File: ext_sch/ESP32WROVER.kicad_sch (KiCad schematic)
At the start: 4 parts, among them U4 ESP32-WROVER

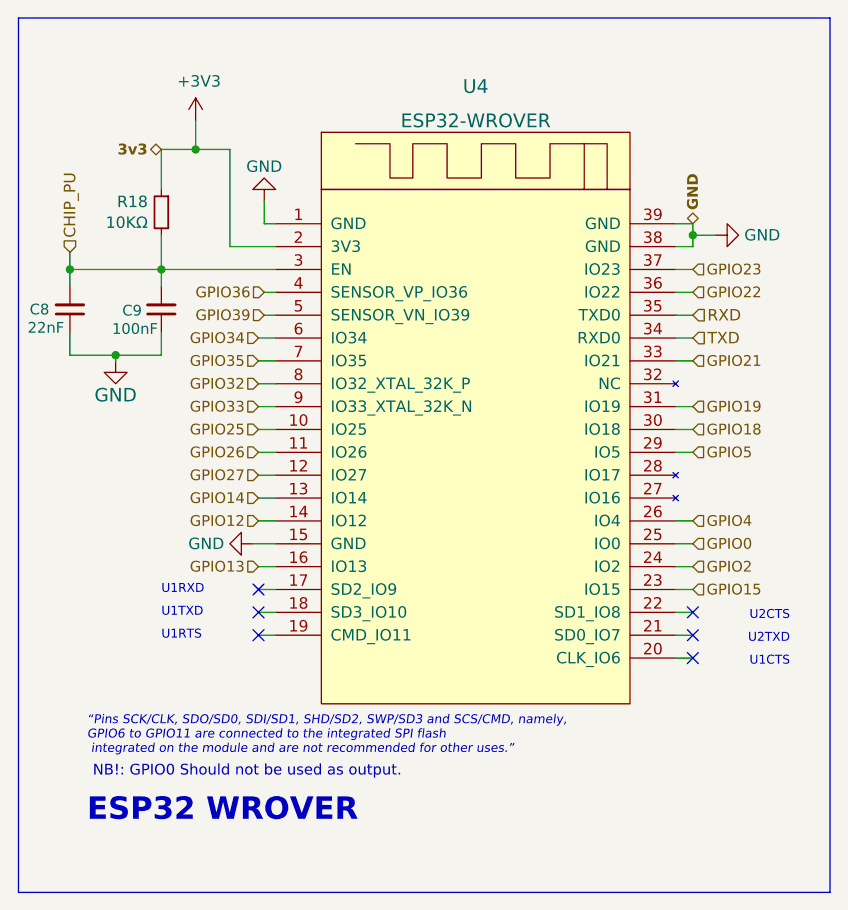
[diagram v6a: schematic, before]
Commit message: Updated all schematic values and parts numbers
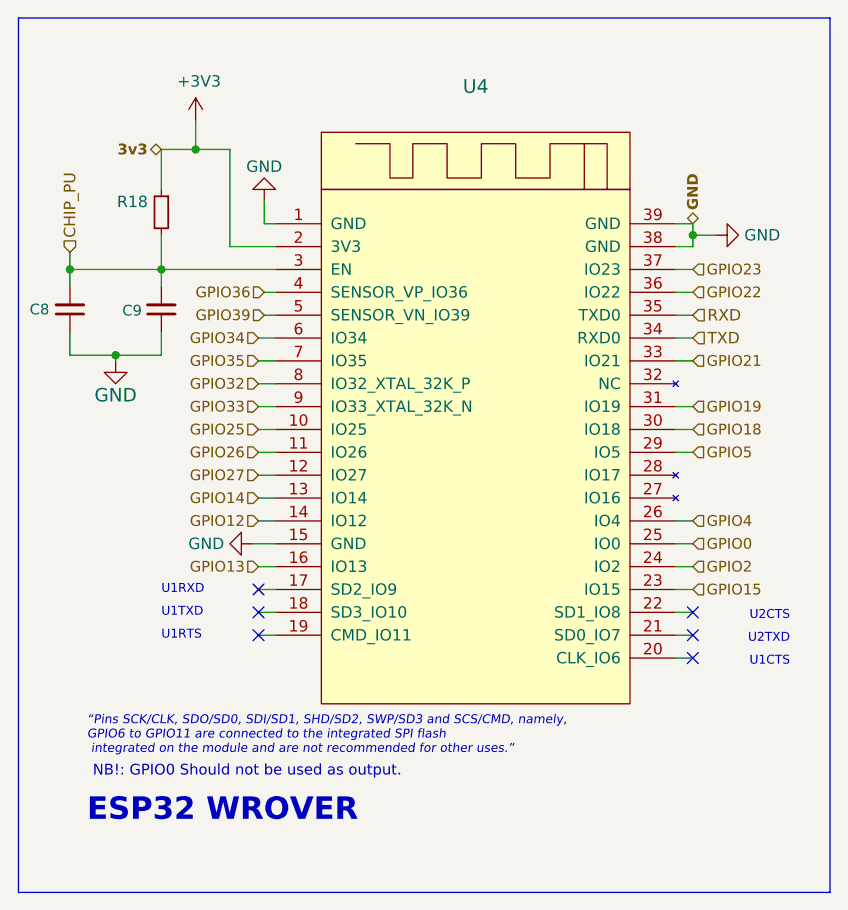
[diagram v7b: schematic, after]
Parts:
- C8: value 22nF -> (none); footprint Capacitor_SMD:C_0603_1608Metric -> (none); LCSC C106222 -> C59461
- C9: value 100nF -> (none); footprint Capacitor_SMD:C_0603_1608Metric -> (none)
- R18: value 10KΩ -> (none); footprint Resistor_SMD:R_0603_1608Metric -> (none)
- U4: value ESP32-WROVER -> (none); footprint Lib:ESP32-WROVER -> (none)
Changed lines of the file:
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@@
       (effects (font (size 1.1938 1.1938)) (justify left))
     )
-    (property "Value" "100nF" (id 1) (at 29.464 48.514 0)
+    (property "Value" "" (id 1) (at 29.464 48.514 0)
       (effects (font (size 1.1938 1.1938)) (justify left))
     )
-    (property "Footprint" "Capacitor_SMD:C_0603_1608Metric" (id 2) (at 29.845 46.355 0)
+    (property "Footprint" "" (id 2) (at 29.845 46.355 0)
       (effects (font (size 1.27 1.27)) hide)
     )
@@
       (effects (font (size 1.27 1.27)) (justify left))
     )
-    (property "Value" "10KΩ" (id 1) (at 28.3464 36.703 0)
+    (property "Value" "" (id 1) (at 28.3464 36.703 0)
       (effects (font (size 1.27 1.27)) (justify left))
     )
-    (property "Footprint" "Resistor_SMD:R_0603_1608Metric" (id 2) (at 29.845 35.56 0)
+    (property "Footprint" "" (id 2) (at 29.845 35.56 0)
       (effects (font (size 1.27 1.27)) hide)
     )
@@
       (effects (font (size 1.1938 1.1938)) (justify left))
     )
-    (property "Value" "22nF" (id 1) (at 19.05 48.387 0)
+    (property "Value" "" (id 1) (at 19.05 48.387 0)
       (effects (font (size 1.1938 1.1938)) (justify left))
     )
-    (property "Footprint" "Capacitor_SMD:C_0603_1608Metric" (id 2) (at 19.685 46.355 0)
+    (property "Footprint" "" (id 2) (at 19.685 46.355 0)
       (effects (font (size 1.27 1.27)) hide)
     )
@@
       (effects (font (size 1.27 1.27)) hide)
     )
-    (property "LCSC" "C106222" (id 4) (at 19.685 46.355 90)
+    (property "LCSC" "C59461" (id 4) (at 19.685 46.355 90)
       (effects (font (size 1.27 1.27)) hide)
     )
@@
       (effects (font (size 1.524 1.524)))
     )
-    (property "Value" "ESP32-WROVER" (id 1) (at 64.77 25.4 0)
+    (property "Value" "" (id 1) (at 64.77 25.4 0)
       (effects (font (size 1.524 1.524)))
     )
-    (property "Footprint" "Lib:ESP32-WROVER" (id 2) (at 76.835 63.5 0)
+    (property "Footprint" "" (id 2) (at 76.835 63.5 0)
       (effects (font (size 1.524 1.524)) hide)
     )

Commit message: Updated readme and pictures!
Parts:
- C8: value (none) -> 22uF; footprint (none) -> Capacitor_SMD:C_0603_1608Metric
- C9: value (none) -> 100nF; footprint (none) -> Capacitor_SMD:C_0603_1608Metric
- R18: value (none) -> 10KΩ; footprint (none) -> Resistor_SMD:R_0603_1608Metric
- U4: value (none) -> ESP32-WROVER; footprint (none) -> Lib:ESP32-WROVER
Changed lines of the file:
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@@
       (effects (font (size 1.1938 1.1938)) (justify left))
     )
-    (property "Value" "" (id 1) (at 29.464 48.514 0)
+    (property "Value" "100nF" (id 1) (at 29.464 48.514 0)
       (effects (font (size 1.1938 1.1938)) (justify left))
     )
-    (property "Footprint" "" (id 2) (at 29.845 46.355 0)
+    (property "Footprint" "Capacitor_SMD:C_0603_1608Metric" (id 2) (at 29.845 46.355 0)
       (effects (font (size 1.27 1.27)) hide)
     )
@@
       (effects (font (size 1.27 1.27)) (justify left))
     )
-    (property "Value" "" (id 1) (at 28.3464 36.703 0)
+    (property "Value" "10KΩ" (id 1) (at 28.3464 36.703 0)
       (effects (font (size 1.27 1.27)) (justify left))
     )
-    (property "Footprint" "" (id 2) (at 29.845 35.56 0)
+    (property "Footprint" "Resistor_SMD:R_0603_1608Metric" (id 2) (at 29.845 35.56 0)
       (effects (font (size 1.27 1.27)) hide)
     )
@@
       (effects (font (size 1.1938 1.1938)) (justify left))
     )
-    (property "Value" "" (id 1) (at 19.05 48.387 0)
+    (property "Value" "22uF" (id 1) (at 19.05 48.387 0)
       (effects (font (size 1.1938 1.1938)) (justify left))
     )
-    (property "Footprint" "" (id 2) (at 19.685 46.355 0)
+    (property "Footprint" "Capacitor_SMD:C_0603_1608Metric" (id 2) (at 19.685 46.355 0)
       (effects (font (size 1.27 1.27)) hide)
     )
@@
       (effects (font (size 1.524 1.524)))
     )
-    (property "Value" "" (id 1) (at 64.77 25.4 0)
+    (property "Value" "ESP32-WROVER" (id 1) (at 64.77 25.4 0)
       (effects (font (size 1.524 1.524)))
     )
-    (property "Footprint" "" (id 2) (at 76.835 63.5 0)
+    (property "Footprint" "Lib:ESP32-WROVER" (id 2) (at 76.835 63.5 0)
       (effects (font (size 1.524 1.524)) hide)
     )
